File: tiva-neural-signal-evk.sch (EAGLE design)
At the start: 112 parts, among them IC1 TM4C123G, IC2 TLV70233, IC3 INA2332, IC4 OPA2320, IC5 OPA2320, IC6 INA2332, IC7 OPA2320, IC8 OPA2320, X1 USB, X2 MICROSD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

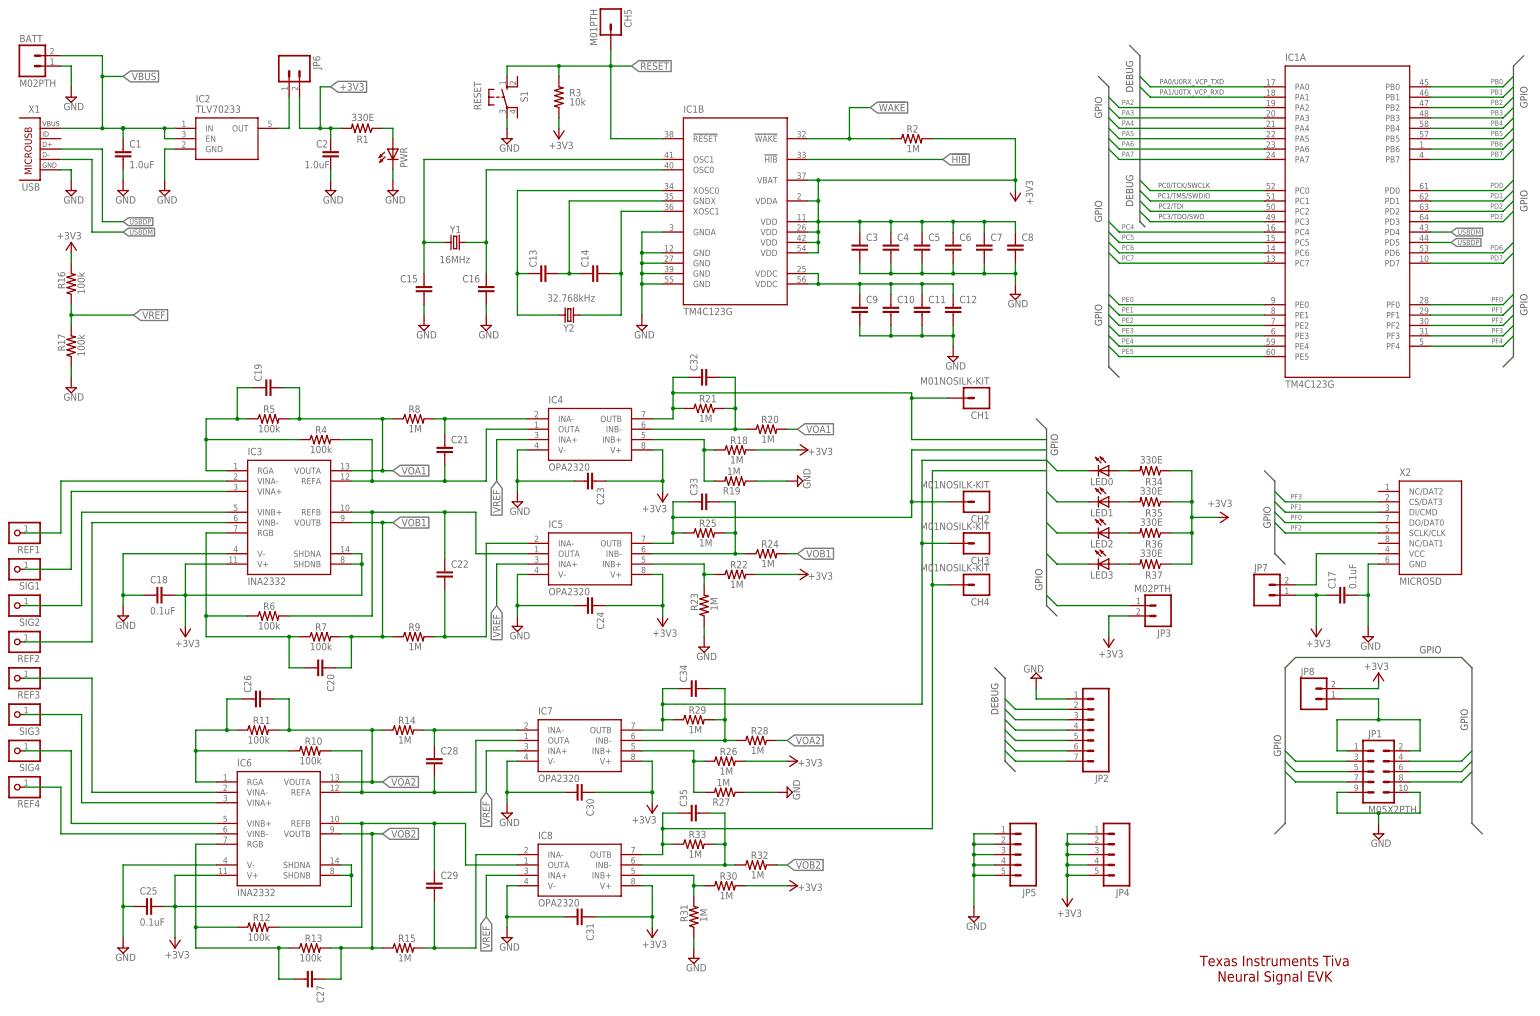
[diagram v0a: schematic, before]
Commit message: added component values
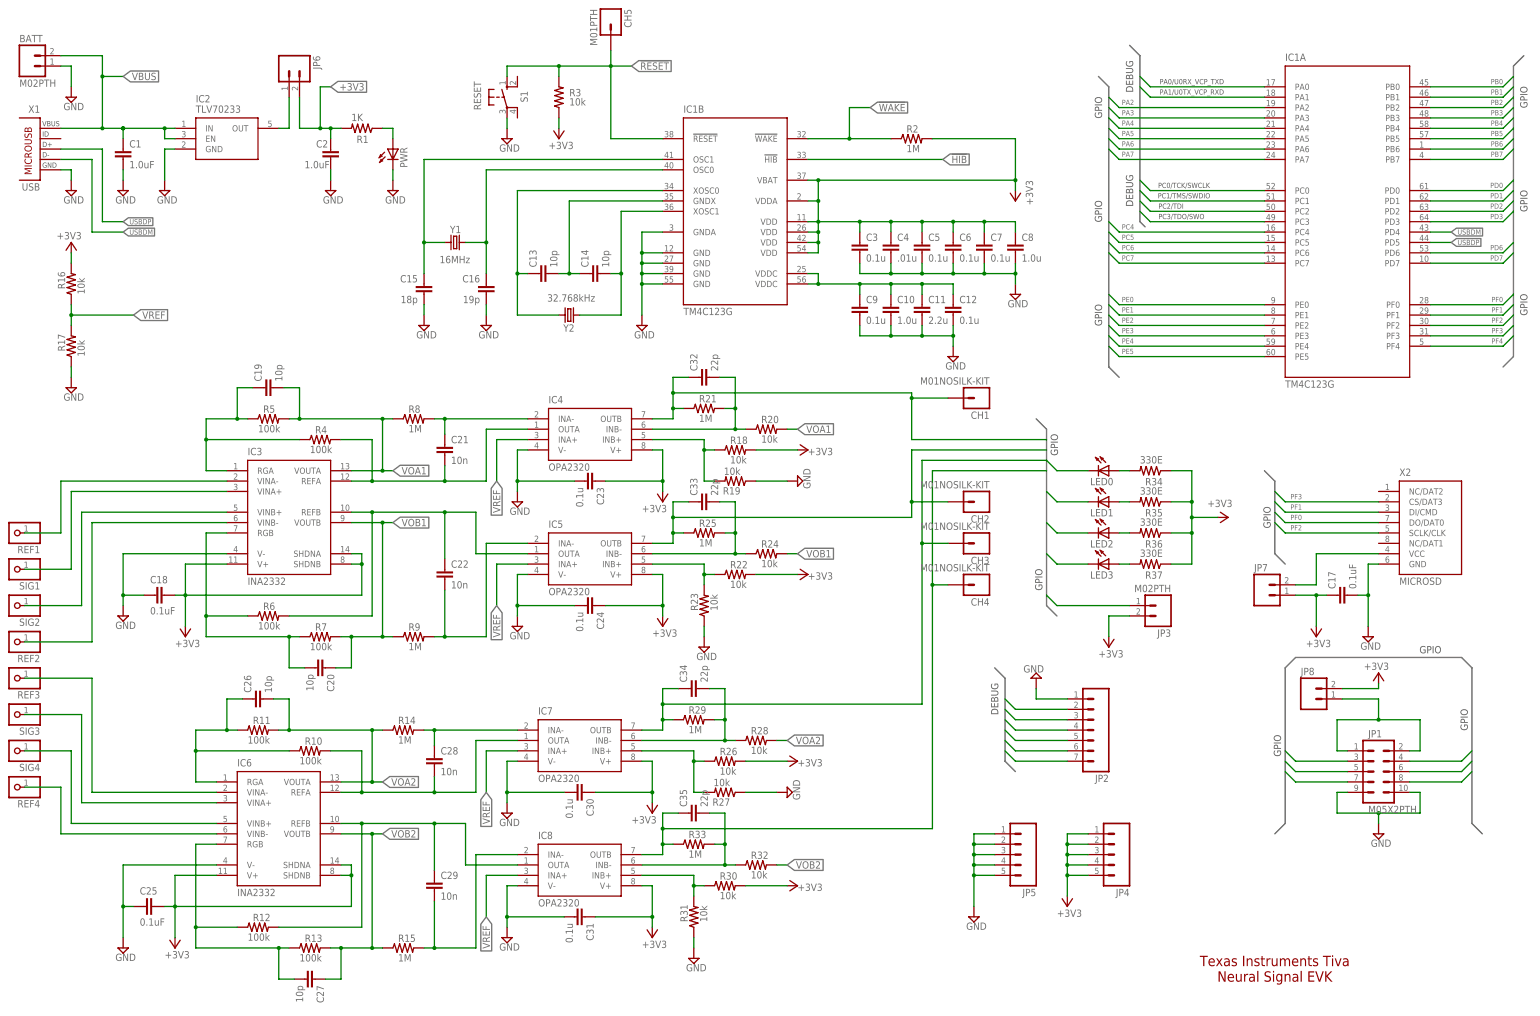
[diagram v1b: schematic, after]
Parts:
- C10, C8: value (none) -> 1.0u
- C11: value (none) -> 2.2u
- C12, C23, C24, C3, C30, C31, C5, C6, C7, C9: value (none) -> 0.1u
- C13, C14, C19, C20, C26, C27: value (none) -> 10p
- C15: value (none) -> 18p
- C16: value (none) -> 19p
- C21, C22, C28, C29: value (none) -> 10n
- C32, C33, C34, C35: value (none) -> 22p
- C4: value (none) -> .01u
- R1: value 330E -> 1K
- R16, R17: value 100k -> 10k
- R18, R19, R20, R22, R23, R24, R26, R27, R28, R30, R31, R32: value 1M -> 10k
